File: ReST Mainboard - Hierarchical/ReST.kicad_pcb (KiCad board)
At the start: 2 copper layers, 100 x 100 mm, 192 parts, among them IC1 AT24C256, P1 CONN_01X02, P10 CONN_02X04, P11 CONN_01X04, P12 CONN_01X04, P13 CONN_01X04, P14 CONN_01X04, P15 USB_OTG, P16 CONN_02X05, P17 CONN_02X05, P18 CONN_02X05, P19 CONN_01X04, P2 CONN_01X03, P20 CONN_01X02, P21 CONN_01X04, P22 CONN_02X03, P23 CONN_02X03, P24 CONN_01X04, P25 CONN_02X03, P26 CONN_02X03, P27 CONN_02X06, P28 CONN_02X02, P29 CONN_01X02, P3 CONN_01X02, P30 CONN_01X02, P31 CONN_01X02, P32 CONN_02X02, P33 CONN_02X02, P34 CONN_02X02, P35 CONN_02X03, P36 CONN_02X03, P37 CONN_02X03, P38 CONN_02X03, P39 CONN_02X03, P4 CONN_01X03, P40 CONN_02X04, P5 CONN_01X03, P6 CONN_01X03, P7 CONN_01X03, P8 CONN_01X03, P9 CONN_01X03, Q1 TBD, Q10 Q_AOT240L, Q11 Q_AOT240L, Q12 Q_AOT240L, Q2 TBD, Q3 TBD, Q4 TBD, Q7 Q_BSH105/IRLML2502, Q8 Q_BSH105/IRLML2502, Q9 Q_BSH105/IRLML2502, U10 USBLC6-2, U2 POLOLU_A4988, U3 ACT4088, U4 SC4626, U5 POLOLU_A4988, U6 POLOLU_A4988, U7 POLOLU_A4988, U8 POLOLU_A4988, U9 STM32F10x/STM32F4x, X1 Crystal_Small

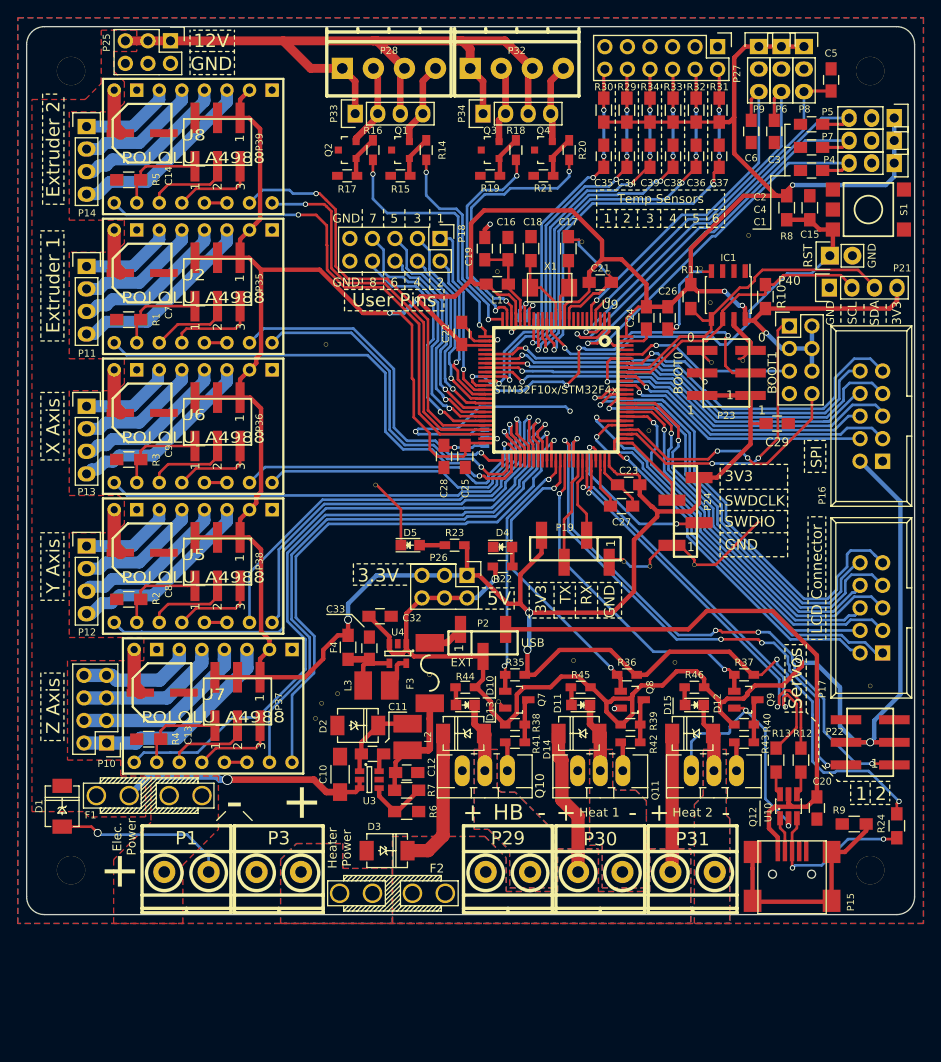
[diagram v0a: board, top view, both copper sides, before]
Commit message: minor changes to values of components and footprints. added two leds for both 12V Rails.
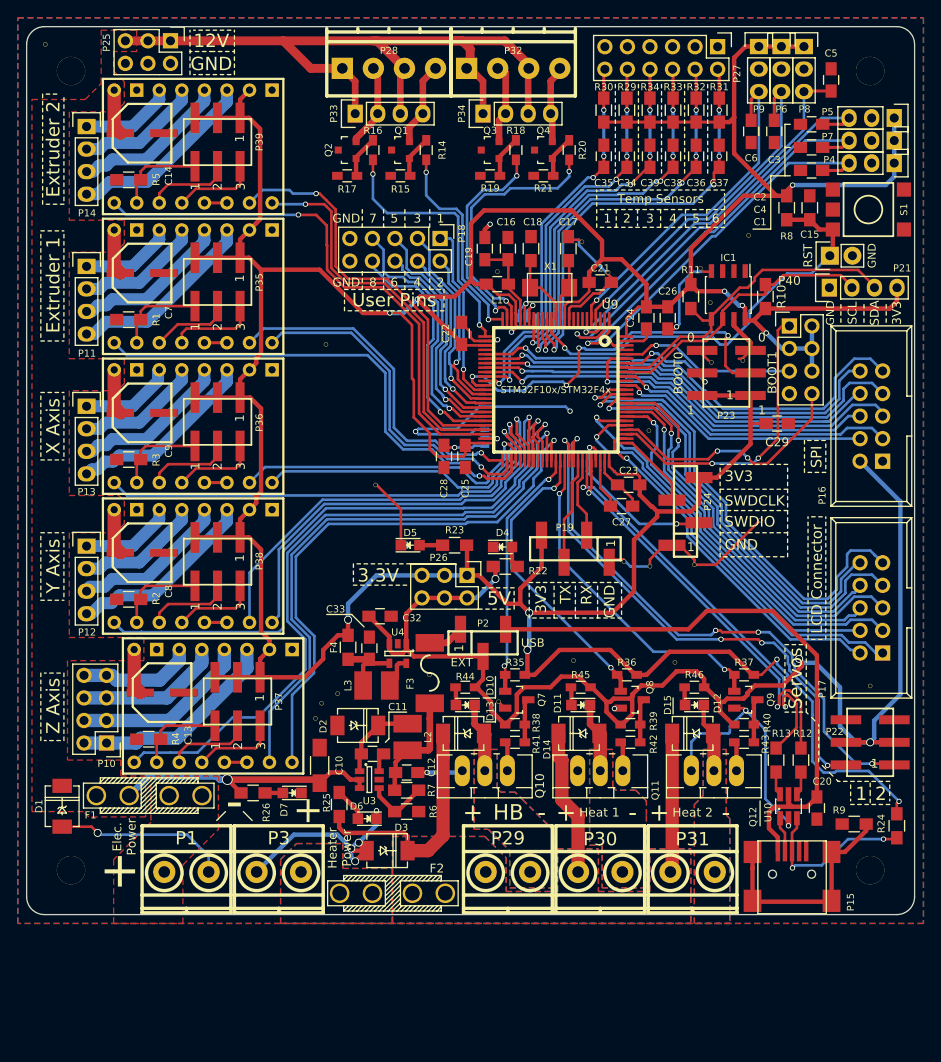
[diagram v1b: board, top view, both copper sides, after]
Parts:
- added D6: LED, LEDs:LED_0805, F.Cu at (57.8, 154.7)
- added D7: LED, LEDs:LED_0805, F.Cu at (49.4, 151.8)
- added R25: 2K, Resistors_SMD:R_0805_HandSoldering, F.Cu at (54.6, 153.1)
- added R26: 2K, Resistors_SMD:R_0805_HandSoldering, F.Cu at (45.0, 151.8)
- added REF**: 1pin, ReST-Library:1pin, F.Cu at (21.6, 67.5)
- R22, R23: value 470R -> 1K; footprint Resistors_SMD:R_0603_HandSoldering -> Resistors_SMD:R_0805_HandSoldering
- R44, R45, R46: value 470R -> 1K
- moved C10 2.51 mm to (52.5, 148.7)
- moved P32 0.40 mm to (74.2, 69.5)
- moved R22 0.30 mm to (73.3, 126.2)
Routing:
- net GND: track 160.5 -> 191.8 mm, vias 10 -> 15
- net +12VA: track 48.4 -> 59.4 mm
- net Net-(D6-Pad2): track 0.00 -> 3.82 mm
- net Net-(D7-Pad2): track 0.00 -> 2.00 mm
- net +12V: track 140.7 -> 142.3 mm

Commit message: final release. PCBs ordered
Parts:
- removed D6, D7: LED, LEDs:LED_0805
- removed R25, R26: 2K, Resistors_SMD:R_0805_HandSoldering
- removed the REF** at (21.6, 67.5)
- removed the REF** at (72.5, 93.0)
- removed the REF** at (58.1, 96.5)
- removed the REF** at (89.5, 111.0)
- removed the REF** at (100.8, 89.0)
- removed the REF** at (53.2, 101.2)
- removed the REF** at (58.8, 117.1)
- removed the REF** at (72.6, 141.5)
- removed the REF** at (52.0, 143.4)
- removed the REF** at (52.7, 141.7)
- removed the REF** at (54.5, 140.6)
- removed the REF** at (114.5, 139.7)
- removed the REF** at (64.8, 138.4)
- removed the REF** at (92.5, 137.1)
- removed the REF** at (81.0, 136.8)
- removed the REF** at (89.7, 126.2)
- removed the REF** at (94.7, 126.0)
- removed the REF** at (102.1, 121.0)
- removed the REF** at (86.7, 125.7)
- removed the REF** at (103.2, 105.8)
- removed the REF** at (100.1, 103.0)
- removed the REF** at (96.6, 103.3)
- removed the REF** at (96.4, 96.5)
- removed the REF** at (95.3, 92.7)
- removed the REF** at (84.9, 93.1)
- removed the REF** at (82.0, 89.7)
- added REF**: 1pin, ReST-Library:1pin, F.Cu at (52.2, 125.6)
- added REF**: 1pin, ReST-Library:1pin, F.Cu at (62.8, 72.5)
- added REF**: 1pin, ReST-Library:1pin, F.Cu at (71.2, 68.3)
- added REF**: 1pin, ReST-Library:1pin, F.Cu at (72.1, 72.6)
- added REF**: 1pin, ReST-Library:1pin, F.Cu at (74.6, 72.4)
- added REF**: 1pin, ReST-Library:1pin, F.Cu at (85.8, 71.7)
- added REF**: 1pin, ReST-Library:1pin, F.Cu at (88.4, 71.7)
- added REF**: 1pin, ReST-Library:1pin, F.Cu at (90.8, 71.7)
- added REF**: 1pin, ReST-Library:1pin, F.Cu at (93.5, 71.8)
- added REF**: 1pin, ReST-Library:1pin, F.Cu at (96.1, 71.8)
- added REF**: 1pin, ReST-Library:1pin, F.Cu at (105.5, 76.3)
- added REF**: 1pin, ReST-Library:1pin, F.Cu at (53.5, 124.6)
- added REF**: 1pin, ReST-Library:1pin, F.Cu at (102.8, 78.5)
- added REF**: 1pin, ReST-Library:1pin, F.Cu at (111.2, 137.5)
- added REF**: 1pin, ReST-Library:1pin, F.Cu at (47.0, 129.5)
- added REF**: 1pin, ReST-Library:1pin, F.Cu at (85.4, 122.3)
- added REF**: 1pin, ReST-Library:1pin, F.Cu at (97.7, 129.3)
- added REF**: 1pin, ReST-Library:1pin, F.Cu at (92.0, 130.5)
- added REF**: 1pin, ReST-Library:1pin, F.Cu at (67.8, 74.9)
- added REF**: 1pin, ReST-Library:1pin, F.Cu at (68.3, 79.0)
- added REF**: 1pin, ReST-Library:1pin, F.Cu at (56.1, 85.3)
- added REF**: 1pin, ReST-Library:1pin, F.Cu at (52.4, 96.7)
- added REF**: 1pin, ReST-Library:1pin, F.Cu at (55.4, 123.1)
- added REF**: 1pin, ReST-Library:1pin, F.Cu at (55.2, 106.6)
- added REF**: 1pin, ReST-Library:1pin, F.Cu at (114.2, 138.7)
- added REF**: 1pin, ReST-Library:1pin, F.Cu at (117.7, 163.8)
- added REF**: 1pin, ReST-Library:1pin, F.Cu at (111.7, 152.1)
- added REF**: 1pin, ReST-Library:1pin, F.Cu at (105.4, 163.8)
- added REF**: 1pin, ReST-Library:1pin, F.Cu at (31.5, 90.0)
- added REF**: 1pin, ReST-Library:1pin, F.Cu at (30.8, 90.7)
- added REF**: 1pin, ReST-Library:1pin, F.Cu at (51.3, 75.1)
- added REF**: 1pin, ReST-Library:1pin, F.Cu at (51.5, 80.3)
- added REF**: 1pin, ReST-Library:1pin, F.Cu at (50.1, 89.9)
- added REF**: 1pin, ReST-Library:1pin, F.Cu at (55.4, 113.1)
- added REF**: 1pin, ReST-Library:1pin, F.Cu at (51.2, 78.5)
- added REF**: 1pin, ReST-Library:1pin, F.Cu at (21.7, 67.5)
- added REF**: 1pin, ReST-Library:1pin, F.Cu at (31.1, 74.8)
- added REF**: 1pin, ReST-Library:1pin, F.Cu at (31.7, 74.0)
- added REF**: 1pin, ReST-Library:1pin, F.Cu at (33.3, 137.4)
- added REF**: 1pin, ReST-Library:1pin, F.Cu at (34.0, 136.9)
- added REF**: 1pin, ReST-Library:1pin, F.Cu at (30.9, 122.2)
- added REF**: 1pin, ReST-Library:1pin, F.Cu at (31.5, 121.5)
- added REF**: 1pin, ReST-Library:1pin, F.Cu at (30.9, 106.2)
- added REF**: 1pin, ReST-Library:1pin, F.Cu at (31.7, 105.5)
- added REF**: 1pin, ReST-Library:1pin, F.Cu at (55.3, 111.2)
- added REF**: 1pin, ReST-Library:1pin, F.Cu at (93.8, 137.1)
- added REF**: 1pin, ReST-Library:1pin, F.Cu at (80.5, 136.9)
- added REF**: 1pin, ReST-Library:1pin, F.Cu at (54.1, 101.3)
- added REF**: 1pin, ReST-Library:1pin, F.Cu at (59.6, 117.2)
- added REF**: 1pin, ReST-Library:1pin, F.Cu at (58.1, 95.8)
- added REF**: 1pin, ReST-Library:1pin, F.Cu at (88.2, 88.3)
- added REF**: 1pin, ReST-Library:1pin, F.Cu at (113.1, 88.2)
- added REF**: 1pin, ReST-Library:1pin, F.Cu at (101.7, 88.9)
- added REF**: 1pin, ReST-Library:1pin, F.Cu at (104.1, 90.4)
- added REF**: 1pin, ReST-Library:1pin, F.Cu at (96.4, 96.5)
- added REF**: 1pin, ReST-Library:1pin, F.Cu at (55.1, 108.8)
- added REF**: 1pin, ReST-Library:1pin, F.Cu at (103.4, 98.7)
- added REF**: 1pin, ReST-Library:1pin, F.Cu at (107.1, 95.5)
- added REF**: 1pin, ReST-Library:1pin, F.Cu at (117.3, 101.2)
- added REF**: 1pin, ReST-Library:1pin, F.Cu at (114.8, 100.9)
- added REF**: 1pin, ReST-Library:1pin, F.Cu at (111.3, 101.2)
- added REF**: 1pin, ReST-Library:1pin, F.Cu at (101.7, 112.9)
- added REF**: 1pin, ReST-Library:1pin, F.Cu at (81.0, 110.2)
- added REF**: 1pin, ReST-Library:1pin, F.Cu at (95.6, 112.7)
- added REF**: 1pin, ReST-Library:1pin, F.Cu at (101.7, 118.0)
- added REF**: 1pin, ReST-Library:1pin, F.Cu at (106.2, 114.8)
- added REF**: 1pin, ReST-Library:1pin, F.Cu at (52.5, 68.4)
- added REF**: 1pin, ReST-Library:1pin, F.Cu at (110.7, 120.2)
- added REF**: 1pin, ReST-Library:1pin, F.Cu at (106.9, 122.0)
- added REF**: 1pin, ReST-Library:1pin, F.Cu at (107.1, 119.5)
- added REF**: 1pin, ReST-Library:1pin, F.Cu at (57.7, 72.6)
- added REF**: 1pin, ReST-Library:1pin, F.Cu at (60.4, 72.4)
- C17, C18: value 30pF -> 10pF
- moved G*** 0.94 mm to (96.4, 131.5)
- moved G*** 0.22 mm to (86.4, 132.3)
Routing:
- net +12VA: track 59.4 -> 48.4 mm
- net (no net): track 0.20 -> 8.66 mm
- net GND: track 191.8 -> 198.3 mm, vias 15 -> 22
- net Net-(D6-Pad2): track 3.82 -> 0.00 mm
- net +12V: track 142.3 -> 140.1 mm
- net Net-(D7-Pad2): track 2.00 -> 0.00 mm
- net Net-(P15-Pad6): track 25.5 -> 27.2 mm

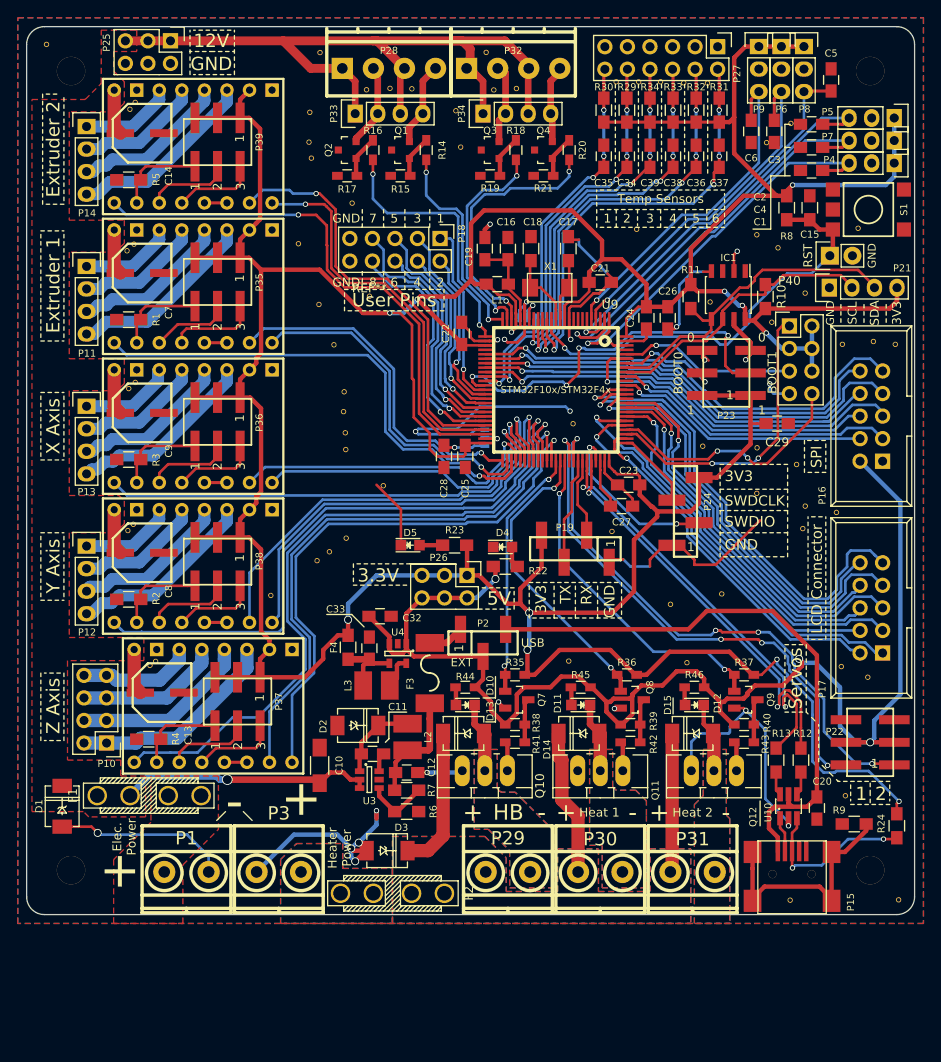
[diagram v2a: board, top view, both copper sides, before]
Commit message: importet new net
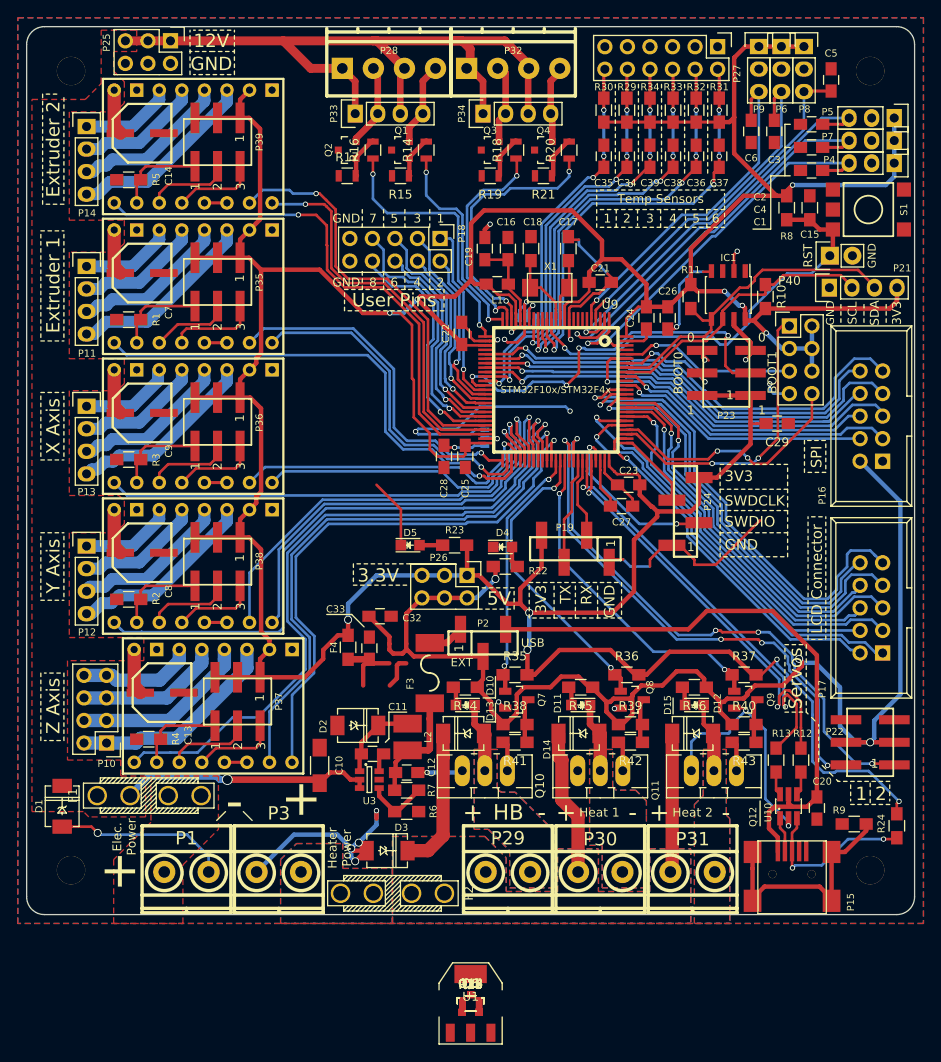
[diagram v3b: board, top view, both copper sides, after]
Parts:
- removed G***: LOGO, ReST-Library:Logo_silk_OSHW_6x6mm
- removed G***: LOGO, ReST-Library:STM32-6mm
- removed L3: 2.2uH, ReST-Library:CD32
- removed the REF** at (52.2, 125.6)
- removed the REF** at (62.8, 72.5)
- removed the REF** at (71.2, 68.3)
- removed the REF** at (72.1, 72.6)
- removed the REF** at (74.6, 72.4)
- removed the REF** at (85.8, 71.7)
- removed the REF** at (88.4, 71.7)
- removed the REF** at (90.8, 71.7)
- removed the REF** at (93.5, 71.8)
- removed the REF** at (96.1, 71.8)
- removed the REF** at (105.5, 76.3)
- removed the REF** at (53.5, 124.6)
- removed the REF** at (102.8, 78.5)
- removed the REF** at (111.2, 137.5)
- removed the REF** at (47.0, 129.5)
- removed the REF** at (85.4, 122.3)
- removed the REF** at (97.7, 129.3)
- removed the REF** at (92.0, 130.5)
- removed the REF** at (67.8, 74.9)
- removed the REF** at (68.3, 79.0)
- removed the REF** at (56.1, 85.3)
- removed the REF** at (52.4, 96.7)
- removed the REF** at (55.4, 123.1)
- removed the REF** at (55.2, 106.6)
- removed the REF** at (114.2, 138.7)
- removed the REF** at (117.7, 163.8)
- removed the REF** at (111.7, 152.1)
- removed the REF** at (105.4, 163.8)
- removed the REF** at (31.5, 90.0)
- removed the REF** at (30.8, 90.7)
- removed the REF** at (51.3, 75.1)
- removed the REF** at (51.5, 80.3)
- removed the REF** at (50.1, 89.9)
- removed the REF** at (55.4, 113.1)
- removed the REF** at (51.2, 78.5)
- removed the REF** at (21.7, 67.5)
- removed the REF** at (31.1, 74.8)
- removed the REF** at (31.7, 74.0)
- removed the REF** at (33.3, 137.4)
- removed the REF** at (34.0, 136.9)
- removed the REF** at (30.9, 122.2)
- removed the REF** at (31.5, 121.5)
- removed the REF** at (30.9, 106.2)
- removed the REF** at (31.7, 105.5)
- removed the REF** at (55.3, 111.2)
- removed the REF** at (93.8, 137.1)
- removed the REF** at (80.5, 136.9)
- removed the REF** at (54.1, 101.3)
- removed the REF** at (59.6, 117.2)
- removed the REF** at (58.1, 95.8)
- removed the REF** at (88.2, 88.3)
- removed the REF** at (113.1, 88.2)
- removed the REF** at (101.7, 88.9)
- removed the REF** at (104.1, 90.4)
- removed the REF** at (96.4, 96.5)
- removed the REF** at (55.1, 108.8)
- removed the REF** at (103.4, 98.7)
- removed the REF** at (107.1, 95.5)
- removed the REF** at (117.3, 101.2)
- removed the REF** at (114.8, 100.9)
- removed the REF** at (111.3, 101.2)
- removed the REF** at (101.7, 112.9)
- removed the REF** at (81.0, 110.2)
- removed the REF** at (95.6, 112.7)
- removed the REF** at (101.7, 118.0)
- removed the REF** at (106.2, 114.8)
- removed the REF** at (52.5, 68.4)
- removed the REF** at (110.7, 120.2)
- removed the REF** at (106.9, 122.0)
- removed the REF** at (107.1, 119.5)
- removed the REF** at (57.7, 72.6)
- removed the REF** at (60.4, 72.4)
- removed U4: SC4626, TO_SOT_Packages_SMD:SOT-23-5
- added Q13, Q14, Q5, Q6: BSS316, TO_SOT_Packages_SMD:SOT-23, F.Cu at (69.5, 175.5)
- added R25, R26, R27, R28: 100K, Resistors_SMD:R_0805, F.Cu at (69.5, 175.5)
- added U1: AMS1117, TO_SOT_Packages_SMD:SOT-223, F.Cu at (69.5, 175.5)
- Q1, Q2, Q3, Q4: value TBD -> BSS138
- Q7, Q8, Q9: value Q_BSH105/IRLML2502 -> BSS138
- R14, R15, R16, R17, R18, R19, R20, R21: footprint Resistors_SMD:R_0603_HandSoldering -> Resistors_SMD:R_0805
- R35, R36, R37, R38, R39, R40, R41, R42, R43, R44, R45, R46: footprint Resistors_SMD:R_0603_HandSoldering -> Resistors_SMD:R_0805_HandSoldering
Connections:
- P15 pad 4: (no net) -> Net-(P15-Pad4)
- Q1 pad 2: /Extra Power Output/EXTRA_1_OUT -> GND
- Q1 pad 3: GND -> /Extra Power Output/EXTRA_0_5V
- Q10 pad 1: /Heater/H0_GATE -> /Heater/HEATER_0_5VL
- Q11 pad 1: /Heater/H1_GATE -> /Heater/HEATER_1_5VL
- Q12 pad 1: /Heater/H2_GATE -> /Heater/HEATER_2_5VL
- Q2 pad 2: /Extra Power Output/EXTRA_0_OUT -> GND
- Q2 pad 3: GND -> /Extra Power Output/EXTRA_2_5V
- Q3 pad 2: /Extra Power Output/EXTRA_2_OUT -> GND
- Q3 pad 3: GND -> /Extra Power Output/EXTRA_1_5V
- Q4 pad 2: /Extra Power Output/EXTRA_3_OUT -> GND
- Q4 pad 3: GND -> /Extra Power Output/EXTRA_3_5V
- Q7 pad 1: HEATER_0 -> /Heater/H0_GATE
- Q8 pad 1: HEATER_1 -> /Heater/H1_GATE
- Q9 pad 1: HEATER_2 -> /Heater/H2_GATE
- R14 pad 2: Net-(Q1-Pad1) -> Net-(Q3-Pad1)
- R15 pad 1: Net-(Q1-Pad1) -> +3V3
- R15 pad 2: GND -> Net-(Q3-Pad1)
- R16 pad 2: Net-(Q2-Pad1) -> Net-(Q1-Pad1)
- R17 pad 1: GND -> Net-(Q1-Pad1)
- R17 pad 2: Net-(Q2-Pad1) -> +3V3
- R18 pad 2: Net-(Q3-Pad1) -> Net-(Q2-Pad1)
- R19 pad 1: Net-(Q3-Pad1) -> +3V3
- R19 pad 2: GND -> Net-(Q2-Pad1)
- R21 pad 1: Net-(Q4-Pad1) -> +3V3
- R21 pad 2: GND -> Net-(Q4-Pad1)
- R41 pad 1: /Heater/HEATER_0_5VL -> HEATER_0
- R42 pad 1: /Heater/HEATER_1_5VL -> HEATER_1
- R43 pad 1: /Heater/HEATER_2_5VL -> HEATER_2
- S1 pad 1: (no net) -> Net-(S1-Pad1)
- U9 pad 29: (no net) -> SPI_CS0
- U9 pad 6: (no net) -> Net-(U9-Pad6)
- U9 pad 7: (no net) -> Net-(U9-Pad7)
- U9 pad 8: (no net) -> Net-(U9-Pad8)
- U9 pad 9: (no net) -> Net-(U9-Pad9)
- U9 pad 90: (no net) -> Net-(U9-Pad90)
- U9 pad 97: (no net) -> Net-(U9-Pad97)
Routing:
- net GND: track 198.3 -> 206.1 mm
- net +3V3: track 531.8 -> 539.5 mm
- net /Extra Power Output/EXTRA_0_OUT: track 9.46 -> 5.64 mm
- net Net-(L3-Pad1): track 3.75 -> 0.00 mm
- net (no net): track 8.66 -> 12.4 mm
- net /Extra Power Output/EXTRA_2_OUT: track 8.76 -> 6.35 mm
- net Net-(Q2-Pad1): track 4.83 -> 2.84 mm
- net Net-(Q1-Pad1): track 4.83 -> 2.84 mm
- net Net-(Q4-Pad1): track 4.83 -> 2.98 mm
- net Net-(Q3-Pad1): track 4.83 -> 2.98 mm
- net /Extra Power Output/EXTRA_1_OUT: track 9.47 -> 7.84 mm
